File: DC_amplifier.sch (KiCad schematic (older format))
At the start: 22 parts, among them Q1 BD136, Q2 BD135, Q3 BD135, Q4 BC337, Q5 BC327, Q6 BDW93A, Q7 BDW94A, U1 TL084

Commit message: Working on TVS.
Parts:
- added D1, D2: 1N4007, Diode_THT:D_DO-41_SOD81_P10.16mm_Horizontal, symbol Diode:1N4007
- added D3, D6: 1.5KE18CA, Diode_THT:D_DO-201AE_P15.24mm_Horizontal, symbol Diode:1.5KExxCA
- added R1: 1000, symbol Device:R
- U1: Spice_Lib_File (none) -> TL084-quad.lib; Spice_Model (none) -> TL084-quad; Spice_Netlist_Enabled (none) -> Y; Spice_Primitive (none) -> X
- V1: Spice_Model dc 18 -> dc 15
- V2: Spice_Model dc -18 -> dc -15
- V3: Spice_Model dc 0 sin(0 10 200k) -> dc 0 sin(0 8 200k)
- renumbered D1 to D4, D2 to D5, R1 to R2, R2 to R3, R3 to R4, R4 to R5, R5 to R6, R6 to R7, R7 to R8
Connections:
- net GND: now also D3.2 (A2), D6.2 (A2)
- net VCC: now also D1.1 (K); no longer V1.1 (E1)
- net VDD: now also D2.2 (A); no longer V2.1 (E1)
- net V_in: now also R1.2; no longer U1.3 (+)
- net V_out: now also D6.1 (A1)
- new net: D1.2 (A), V1.1 (E1)
- new net: D2.1 (K), V2.1 (E1)
- new net: D3.1 (A1), R1.1, U1.3 (+)
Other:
- moved on the sheet: C1, D4, D5, Q1, Q2, Q3, Q4, Q5, Q6, Q7, R2, R3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

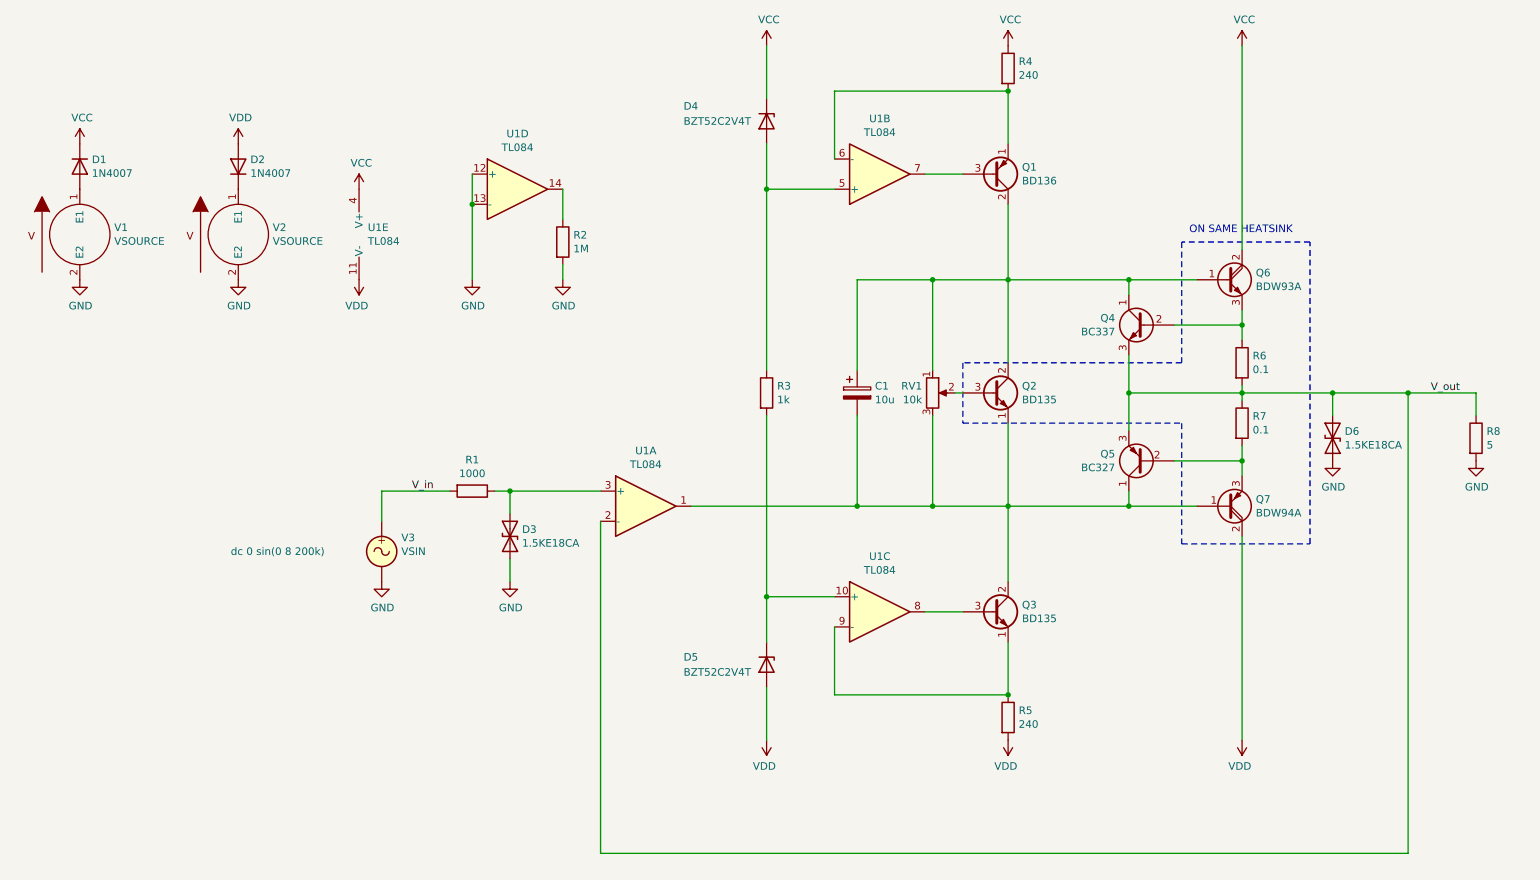
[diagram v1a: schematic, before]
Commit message: Mirrored VBE multipliers
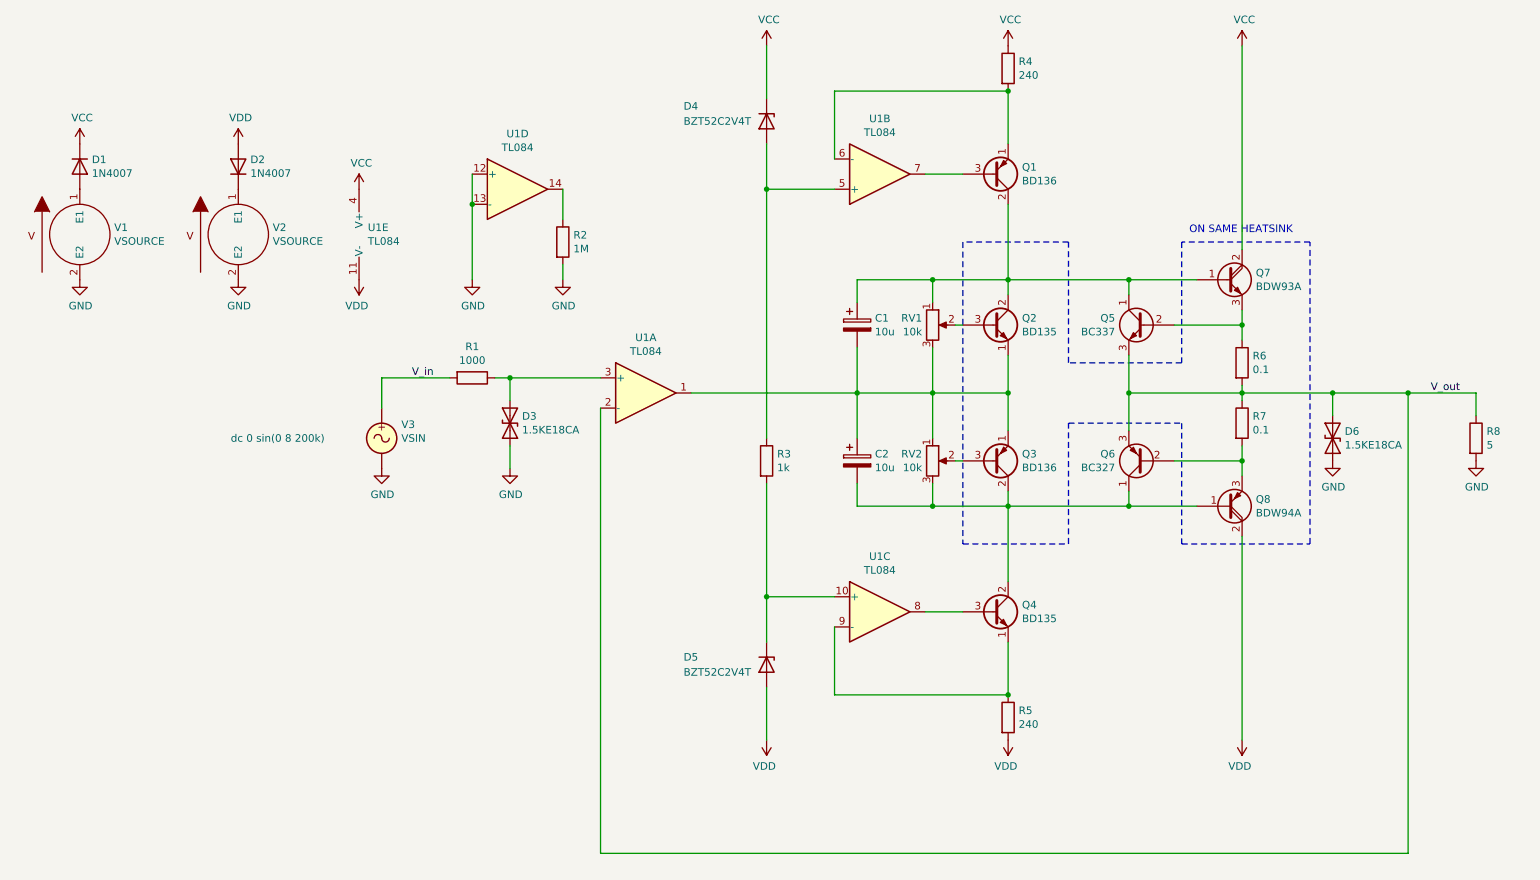
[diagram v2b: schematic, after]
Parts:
- added C2: 10u, symbol Device:CP
- added Q3: BD136, Package_TO_SOT_THT:TO-126-3_Vertical, symbol Transistor_BJT:BD136
- added RV2: 10k, symbol Device:R_POT
- renumbered Q3 to Q4, Q4 to Q5, Q5 to Q6, Q6 to Q7, Q7 to Q8
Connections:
- net at C1.2, Q2.1 (E), RV1.3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: now also C2.1, Q3.1 (E), RV2.1; no longer Q4.2 (C), Q6.1 (C), Q8.1 (B)
- new net: C2.2, Q3.2 (C), Q4.2 (C), Q6.1 (C), Q8.1 (B), RV2.3
- new net: Q3.3 (B), RV2.2
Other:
- moved on the sheet: C1, D3, Q2, R1, R3, RV1, U1A, V3

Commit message: Working on VBE multipliers: understanding correct bias.
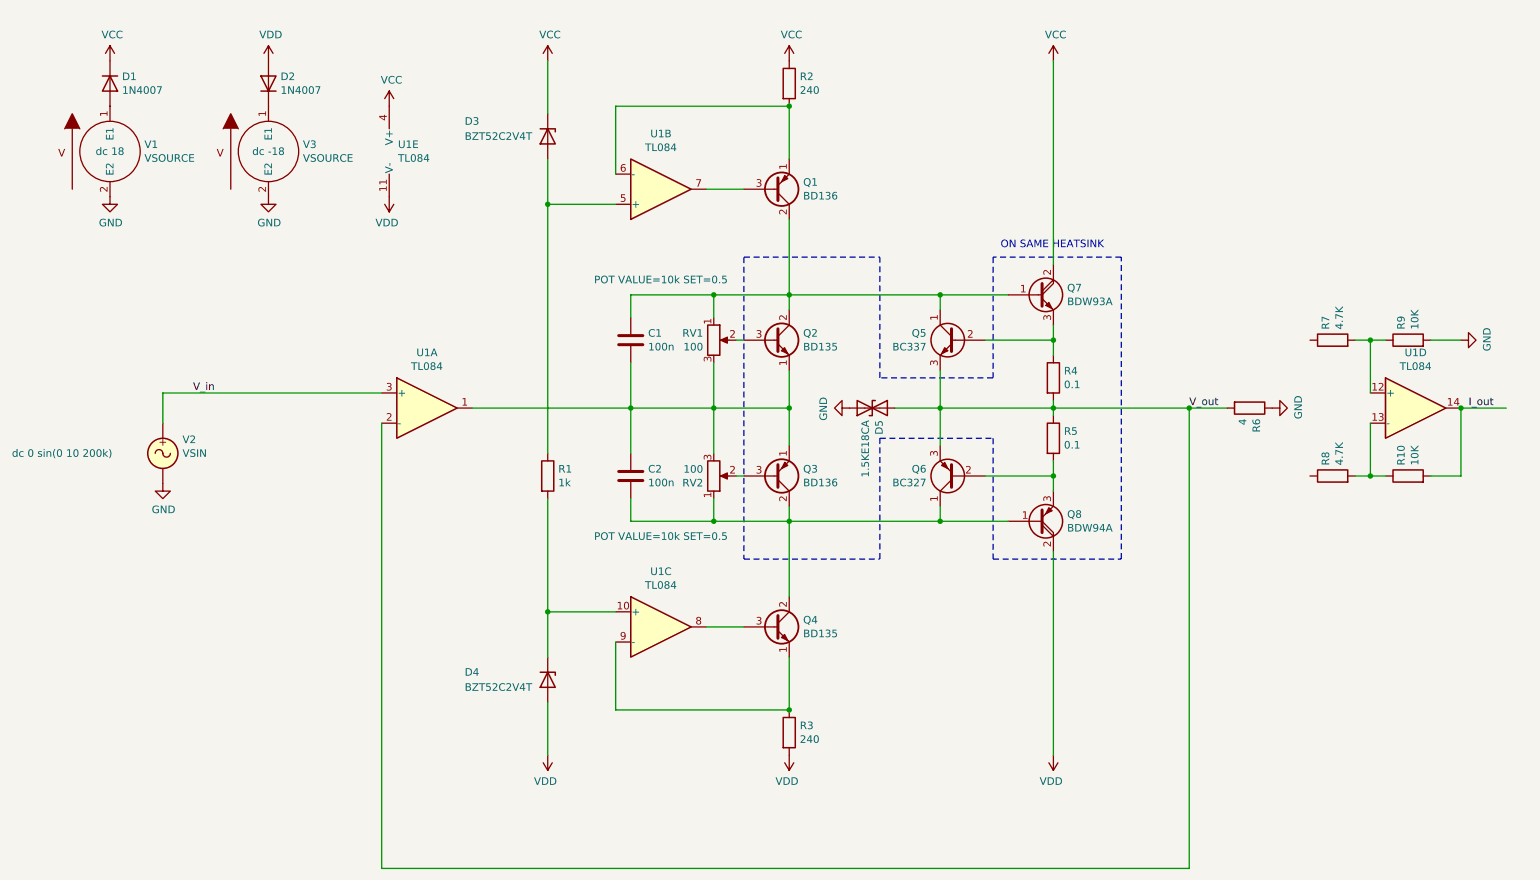
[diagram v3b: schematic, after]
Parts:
- removed C1, C2: 10u, symbol Device:CP
- removed D3: 1.5KE18CA, Diode_THT:D_DO-201AE_P15.24mm_Horizontal, symbol Diode:1.5KExxCA
- removed R1: 1000, symbol Device:R
- added C1, C2: 100n, symbol Device:C
- added R10, R9: 10K, symbol Device:R
- added R8: 4.7K, symbol Device:R
- R6: renamed from R8; value 5 -> 4
- R7: renamed from R2; value 1M -> 4.7K
- RV1, RV2: value 10k -> 100; Spice_Model POT VALUE=10k SET=0.27 -> POT VALUE=10k SET=0.5
- V1: Spice_Model dc 15 -> dc 18
- V2: renamed from V3; Spice_Model dc 0 sin(0 8 200k) -> dc 0 sin(0 10 200k)
- V3: renamed from V2; Spice_Model dc -15 -> dc -18
- renumbered D4 to D3, D5 to D4, D6 to D5, R3 to R1, R4 to R2, R5 to R3, R6 to R4, R7 to R5
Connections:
- net GND: now also R6.1, R9.2; no longer R6.2, R7.2, U1.12 (+), U1.13 (-)
- net V_in: now also U1.3 (+)
- net V_out: now also R6.2; no longer R6.1
- net at Q1.2 (C), Q2.2 (C), Q5.1 (C)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: now also C1.1
- net at Q2.1 (E), Q3.1 (E), RV1.3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: now also RV2.3, C1.2, C2.1; no longer RV2.1
- net at Q3.2 (C), Q4.2 (C), Q6.1 (C)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: now also RV2.1, C2.2; no longer RV2.3
- net at R7.1: no longer U1.14
- new net: R7.2, R9.1, U1.12 (+)
- new net: R10.1, R8.2, U1.13 (-)
- new net I_out: R10.2, U1.14
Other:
- moved on the sheet: D1, D2, D3, D4, D5, Q1, Q2, Q3, Q4, Q5, Q6, Q7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

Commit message: Added current monitor.
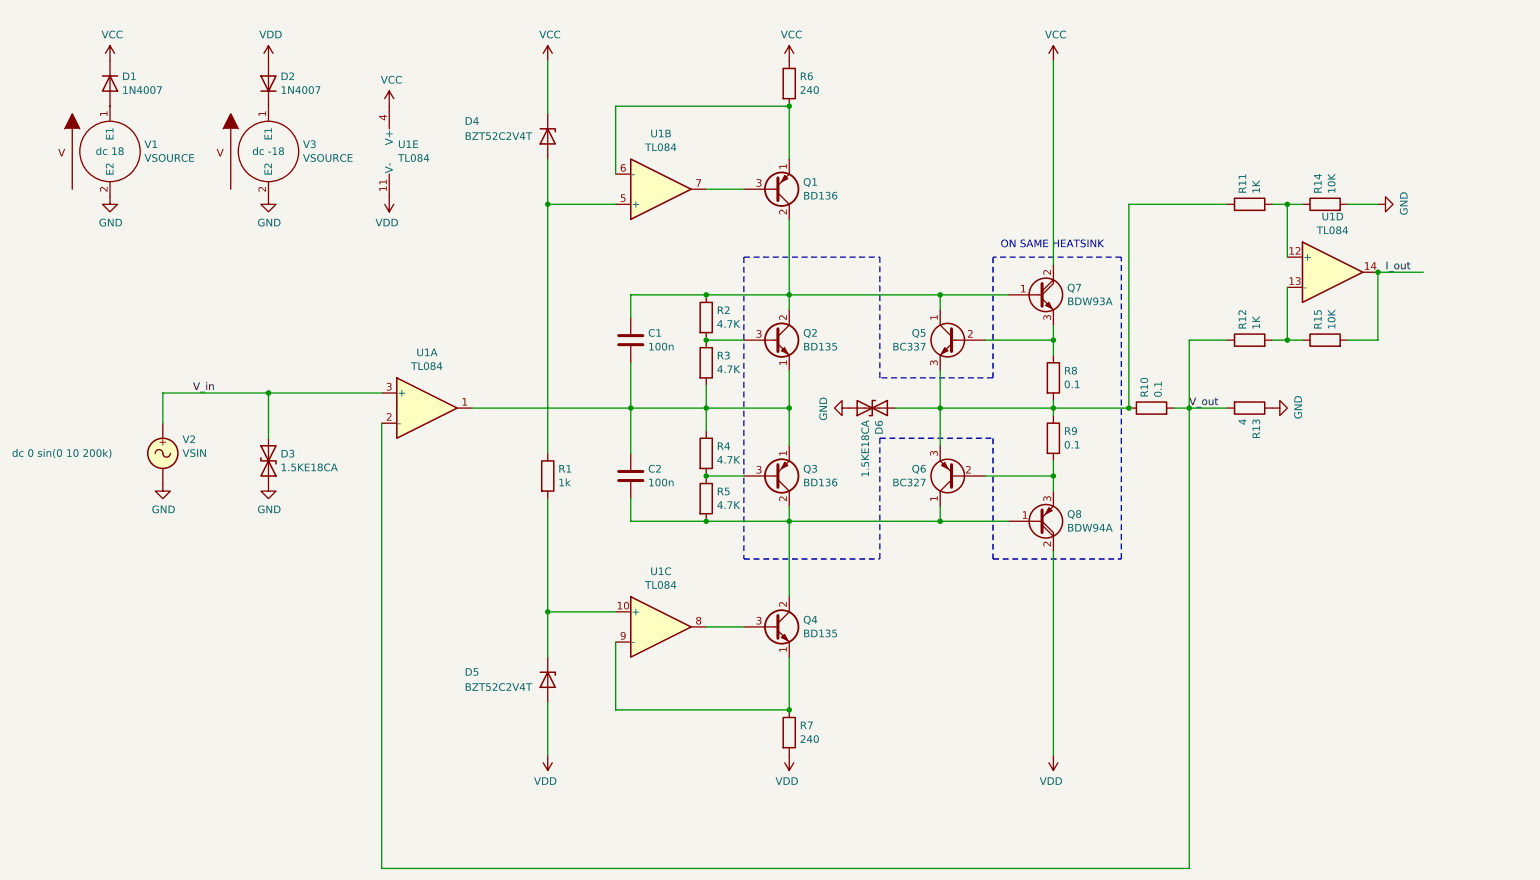
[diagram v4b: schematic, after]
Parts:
- removed RV1, RV2: 100, symbol Device:R_POT
- added D3: 1.5KE18CA, Diode_THT:D_DO-201AE_P15.24mm_Horizontal, symbol Diode:1.5KExxCA
- added R10: 0.1, symbol Device:R
- added R2, R3, R4, R5: 4.7K, symbol Device:R
- R11: renamed from R7; value 4.7K -> 1K
- R12: renamed from R8; value 4.7K -> 1K
- renumbered D3 to D4, D4 to D5, D5 to D6, R6 to R13, R9 to R14, R10 to R15, R2 to R6, R3 to R7, R4 to R8, R5 to R9
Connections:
- net GND: now also D3.2 (A2)
- net V_in: now also D3.1 (A1)
- net V_out: now also R12.1, R10.2; no longer D6.1 (A1), Q5.3 (E), Q6.3 (E), R8.2, R9.1
- net at C1.2, C2.1, Q2.1 (E)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: now also R3.2, R4.1
- net at C1.1, Q1.2 (C), Q2.2 (C)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: now also R2.1
- net at Q2.3 (B): now also R2.2, R3.1
- net at C2.2, Q3.2 (C), Q4.2 (C)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: now also R5.2
- net at R11.1: now also D6.1 (A1), Q5.3 (E), Q6.3 (E), R8.2, R9.1, R10.1
- net at Q3.3 (B): now also R4.2, R5.1
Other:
- moved on the sheet: R11, R12, R14, R15, U1D
